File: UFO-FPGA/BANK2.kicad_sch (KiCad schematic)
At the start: 12 parts, among them U1 ICE40HX8K-BG121

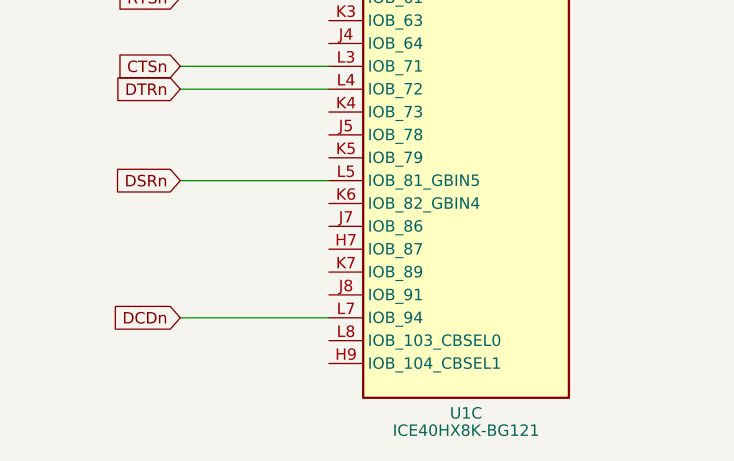
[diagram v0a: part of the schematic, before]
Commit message: PCB planes
Added:
added Power plane +1v2, +3v3 and +5v on layer 4
Ground plane on layer 2 and 5
Added signal layer 1,3 and 6
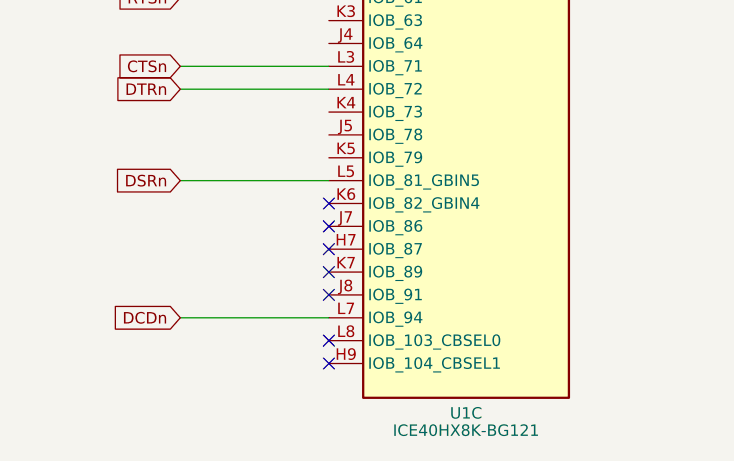
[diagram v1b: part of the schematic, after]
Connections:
- no-connect marks 0 -> 7
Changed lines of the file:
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@@
   (junction (at 161.925 52.07) (diameter 0) (color 0 0 0 0)
   )
+  (no_connect (at 111.125 123.19))
+  (no_connect (at 111.125 125.73))
+  (no_connect (at 111.125 115.57))
+  (no_connect (at 111.125 110.49))
+  (no_connect (at 111.125 113.03))
+  (no_connect (at 111.125 107.95))
+  (no_connect (at 111.125 118.11))
   (wire (pts (xy 94.615 80.01) (xy 111.125 80.01))
     (stroke (width 0) (type default))

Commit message: PCB
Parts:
- TP7, TP8: footprint TestPoint:TestPoint_Keystone_5000-5004_Miniature -> TestPoint:TestPoint_Pad_1.5x1.5mm
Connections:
- net +1V2 is gone; now on net +3V3: R25.1
- net CTSn: no longer U1.L3 (IOB_71)
- net DCDn: no longer U1.L7 (IOB_94)
- net DSRn: no longer U1.L5 (IOB_81_GBIN5)
- net DTRn: no longer U1.L4 (IOB_72)
- net RS232_Rx_TTL: no longer U1.L1 (IOB_56)
- net RTSn: no longer U1.L2 (IOB_61)
- no-connect marks 7 -> 13
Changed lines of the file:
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@@
   )
   (no_connect (at 111.125 123.19))
+  (no_connect (at 111.125 102.87))
   (no_connect (at 111.125 125.73))
+  (no_connect (at 111.125 87.63))
   (no_connect (at 111.125 115.57))
   (no_connect (at 111.125 110.49))
+  (no_connect (at 111.125 107.95))
   (no_connect (at 111.125 113.03))
-  (no_connect (at 111.125 107.95))
+  (no_connect (at 111.125 100.33))
+  (no_connect (at 111.125 90.17))
+  (no_connect (at 111.125 82.55))
   (no_connect (at 111.125 118.11))
+  (no_connect (at 111.125 97.79))
   (wire (pts (xy 94.615 80.01) (xy 111.125 80.01))
     (stroke (width 0) (type default))
@@
     (stroke (width 0) (type default))
   )
+  (wire (pts (xy 174.625 52.07) (xy 173.355 52.07))
+    (stroke (width 0) (type default))
+  )
+  (wire (pts (xy 139.065 52.07) (xy 126.365 52.07))
+    (stroke (width 0) (type default))
+  )
+  (wire (pts (xy 94.615 105.41) (xy 111.125 105.41))
+    (stroke (width 0) (type default))
+  )
+  (wire (pts (xy 161.925 52.07) (xy 150.495 52.07))
+    (stroke (width 0) (type default))
+  )
+  (wire (pts (xy 94.615 120.65) (xy 111.125 120.65))
+    (stroke (width 0) (type default))
+  )
+  (wire (pts (xy 94.615 72.39) (xy 102.235 72.39))
+    (stroke (width 0) (type default))
+  )
+  (wire (pts (xy 161.925 59.69) (xy 173.355 59.69))
+    (stroke (width 0) (type default))
+  )
+  (wire (pts (xy 150.495 52.07) (xy 139.065 52.07))
+    (stroke (width 0) (type default))
+  )
+  (wire (pts (xy 178.435 60.325) (xy 178.435 62.865))
+    (stroke (width 0) (type default))
+  )
+  (wire (pts (xy 102.235 72.39) (xy 111.125 72.39))
+    (stroke (width 0) (type default))
+  )
+  (wire (pts (xy 94.615 92.71) (xy 111.125 92.71))
+    (stroke (width 0) (type default))
+  )
+  (wire (pts (xy 150.495 59.69) (xy 139.065 59.69))
+    (stroke (width 0) (type default))
+  )
   (wire (pts (xy 192.405 41.91) (xy 192.405 52.07))
-    (stroke (width 0) (type default))
-  )
-  (wire (pts (xy 174.625 52.07) (xy 173.355 52.07))
-    (stroke (width 0) (type default))
-  )
-  (wire (pts (xy 139.065 52.07) (xy 126.365 52.07))
-    (stroke (width 0) (type default))
-  )
-  (wire (pts (xy 94.615 105.41) (xy 111.125 105.41))
-    (stroke (width 0) (type default))
-  )
-  (wire (pts (xy 161.925 52.07) (xy 150.495 52.07))
-    (stroke (width 0) (type default))
-  )
-  (wire (pts (xy 94.615 120.65) (xy 111.125 120.65))
-    (stroke (width 0) (type default))
-  )
-  (wire (pts (xy 94.615 72.39) (xy 102.235 72.39))
-    (stroke (width 0) (type default))
-  )
-  (wire (pts (xy 161.925 59.69) (xy 173.355 59.69))
-    (stroke (width 0) (type default))
-  )
-  (wire (pts (xy 150.495 52.07) (xy 139.065 52.07))
-    (stroke (width 0) (type default))
-  )
-  (wire (pts (xy 178.435 60.325) (xy 178.435 62.865))
-    (stroke (width 0) (type default))
-  )
-  (wire (pts (xy 102.235 72.39) (xy 111.125 72.39))
-    (stroke (width 0) (type default))
-  )
-  (wire (pts (xy 94.615 92.71) (xy 111.125 92.71))
-    (stroke (width 0) (type default))
-  )
-  (wire (pts (xy 150.495 59.69) (xy 139.065 59.69))
     (stroke (width 0) (type default))
   )
@@
     (effects (font (size 1.27 1.27)) (justify left bottom))
   )
-  (global_label "CTSn" (shape input) (at 94.615 92.71 180) (fields_autoplaced)
+  (global_label "CTSn" (shape input) (at 86.36 92.71 180) (fields_autoplaced)
     (effects (font (size 1.27 1.27)) (justify right))
-    (property "Intersheetrefs" "${INTERSHEET_REFS}" (at 87.1131 92.71 0)
+    (property "Intersheetrefs" "${INTERSHEET_REFS}" (at 78.8581 92.71 0)
       (effects (font (size 1.27 1.27)) (justify right) hide)
     )
   )
-  (global_label "DCDn" (shape input) (at 94.615 120.65 180) (fields_autoplaced)
+  (global_label "DCDn" (shape input) (at 86.36 120.65 180) (fields_autoplaced)
     (effects (font (size 1.27 1.27)) (justify right))
-    (property "Intersheetrefs" "${INTERSHEET_REFS}" (at 86.7502 120.65 0)
+    (property "Intersheetrefs" "${INTERSHEET_REFS}" (at 78.4952 120.65 0)
       (effects (font (size 1.27 1.27)) (justify right) hide)
     )
@@
     )
   )
-  (global_label "DTRn" (shape input) (at 94.615 95.25 180) (fields_autoplaced)
+  (global_label "DTRn" (shape input) (at 86.36 95.25 180) (fields_autoplaced)
     (effects (font (size 1.27 1.27)) (justify right))
-    (property "Intersheetrefs" "${INTERSHEET_REFS}" (at 87.0526 95.25 0)
+    (property "Intersheetrefs" "${INTERSHEET_REFS}" (at 78.7976 95.25 0)
       (effects (font (size 1.27 1.27)) (justify right) hide)
     )
   )
-  (global_label "RS232_Rx_TTL" (shape input) (at 94.615 80.01 180) (fields_autoplaced)
+  (global_label "RS232_Rx_TTL" (shape input) (at 86.36 80.01 180) (fields_autoplaced)
     (effects (font (size 1.27 1.27)) (justify right))
-    (property "Intersheetrefs" "${INTERSHEET_REFS}" (at 78.4046 80.01 0)
+    (property "Intersheetrefs" "${INTERSHEET_REFS}" (at 70.1496 80.01 0)
       (effects (font (size 1.27 1.27)) (justify right) hide)
     )
   )
-  (global_label "DSRn" (shape input) (at 94.615 105.41 180) (fields_autoplaced)
+  (global_label "DSRn" (shape input) (at 86.36 105.41 180) (fields_autoplaced)
     (effects (font (size 1.27 1.27)) (justify right))
-    (property "Intersheetrefs" "${INTERSHEET_REFS}" (at 86.8107 105.41 0)
+    (property "Intersheetrefs" "${INTERSHEET_REFS}" (at 78.5557 105.41 0)
       (effects (font (size 1.27 1.27)) (justify right) hide)
     )
   )
-  (global_label "RTSn" (shape input) (at 94.615 85.09 180) (fields_autoplaced)
+  (global_label "RTSn" (shape input) (at 86.36 85.09 180) (fields_autoplaced)
     (effects (font (size 1.27 1.27)) (justify right))
-    (property "Intersheetrefs" "${INTERSHEET_REFS}" (at 87.1131 85.09 0)
+    (property "Intersheetrefs" "${INTERSHEET_REFS}" (at 78.8581 85.09 0)
       (effects (font (size 1.27 1.27)) (justify right) hide)
     )
@@
     )
   )
+  (symbol (lib_id "power:+3V3") (at 192.405 41.91 0) (unit 1)
+    (in_bom yes) (on_board yes) (dnp no) (fields_autoplaced)
+    (property "Reference" "#PWR062" (at 192.405 45.72 0)
+      (effects (font (size 1.27 1.27)) hide)
+    )
+    (property "Value" "+3V3" (at 192.405 38.4081 0)
+      (effects (font (size 1.27 1.27)))
+    )
+    (property "Footprint" "" (at 192.405 41.91 0)
+      (effects (font (size 1.27 1.27)) hide)
+    )
+    (property "Datasheet" "" (at 192.405 41.91 0)
+      (effects (font (size 1.27 1.27)) hide)
+    )
+    (pin "1")
+    (instances
+      (project "UFO-FPGA"
+        (path "/b3168f6a-c732-41d3-aeeb-d97dd2f1bb65/03eb349d-f783-448d-a9ad-735fd21dbf61"
+          (reference "#PWR062") (unit 1)
+        )
+        (path "/b3168f6a-c732-41d3-aeeb-d97dd2f1bb65/6f7e0d88-d92b-4c4f-9dc8-64721cd46d41"
+          (reference "#PWR076") (unit 1)
+        )
+      )
+    )
+  )
   (symbol (lib_id "Device:C") (at 139.065 55.88 0) (mirror y) (unit 1)
     (in_bom yes) (on_board yes) (dnp no) (fields_autoplaced)
@@
         (path "/b3168f6a-c732-41d3-aeeb-d97dd2f1bb65/6f7e0d88-d92b-4c4f-9dc8-64721cd46d41"
           (reference "R27") (unit 1)
-        )
-      )
-    )
-  )
-  (symbol (lib_id "power:+1V2") (at 192.405 41.91 0) (unit 1)
-    (in_bom yes) (on_board yes) (dnp no) (fields_autoplaced)
-    (property "Reference" "#PWR024" (at 192.405 45.72 0)
-      (effects (font (size 1.27 1.27)) hide)
-    )
-    (property "Value" "+1V2" (at 192.405 38.4081 0)
-      (effects (font (size 1.27 1.27)))
-    )
-    (property "Footprint" "" (at 192.405 41.91 0)
-      (effects (font (size 1.27 1.27)) hide)
-    )
-    (property "Datasheet" "" (at 192.405 41.91 0)
-      (effects (font (size 1.27 1.27)) hide)
-    )
-    (pin "1")
-    (instances
-      (project "UFO-FPGA"
-        (path "/b3168f6a-c732-41d3-aeeb-d97dd2f1bb65/a9a0295d-b075-4952-a5ba-04debc5f691c"
-          (reference "#PWR024") (unit 1)
-        )
-        (path "/b3168f6a-c732-41d3-aeeb-d97dd2f1bb65/03eb349d-f783-448d-a9ad-735fd21dbf61"
-          (reference "#PWR027") (unit 1)
-        )
-        (path "/b3168f6a-c732-41d3-aeeb-d97dd2f1bb65/6f7e0d88-d92b-4c4f-9dc8-64721cd46d41"
-          (reference "#PWR078") (unit 1)
         )
       )
@@
       (effects (font (size 1.27 1.27)) (justify left))
     )
-    (property "Footprint" "TestPoint:TestPoint_Keystone_5000-5004_Miniature" (at 179.705 52.07 0)
+    (property "Footprint" "TestPoint:TestPoint_Pad_1.5x1.5mm" (at 179.705 52.07 0)
       (effects (font (size 1.27 1.27)) hide)
     )
@@
       (effects (font (size 1.27 1.27)) (justify right))
     )
-    (property "Footprint" "TestPoint:TestPoint_Keystone_5000-5004_Miniature" (at 97.155 72.39 0)
-      (effects (font (size 1.27 1.27)) hide)
-    )
+    (property "Footprint" "TestPoint:TestPoint_Pad_1.5x1.5mm" (at 97.155 72.39 0)
+      (effects (font (size 1.27 1.27)) hide)
+    )

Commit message: PCB
many pcb changes
-started routing
-added vias
-power planes
-ground planes
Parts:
- removed C17 (x3): 100nF, Capacitor_SMD:C_0805_2012Metric_Pad1.18x1.45mm_HandSolder, symbol Device:C
- removed R25: 130R, Resistor_SMD:R_0805_2012Metric_Pad1.20x1.40mm_HandSolder, symbol Device:R
- removed R25: 1R, Resistor_SMD:R_0805_2012Metric_Pad1.20x1.40mm_HandSolder, symbol Device:R
- added C17: 200nF, Capacitor_SMD:C_0805_2012Metric_Pad1.18x1.45mm_HandSolder, symbol Device:C
- added R29: 0, Resistor_SMD:R_0805_2012Metric_Pad1.20x1.40mm_HandSolder, symbol Device:R
- C18: value 100nF -> 200nF
- R25: value 510R -> 690R
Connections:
- net +3V3: now also R29.2
- net GND: now also C17.2
- net ICE_CDONE: now also R25.2
- net VCCIO_2: now also C17.1, R29.1
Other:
- moved on the sheet: R25

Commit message: pcb prog redesign
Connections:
- net ICE_CLK: now reaches U1.K6 (IOB_82_GBIN4)
- no-connect marks 13 -> 12
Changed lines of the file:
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@@
   (no_connect (at 111.125 115.57))
   (no_connect (at 111.125 110.49))
-  (no_connect (at 111.125 107.95))
   (no_connect (at 111.125 113.03))
   (no_connect (at 111.125 100.33))
@@
   )
   (wire (pts (xy 189.23 52.07) (xy 192.405 52.07))
+    (stroke (width 0) (type default))
+  )
+  (wire (pts (xy 86.36 107.95) (xy 111.125 107.95))
     (stroke (width 0) (type default))
   )
@@
       (effects (font (size 1.27 1.27)) (justify right) hide)
     )
+  )
+  (global_label "ICE_CLK" (shape input) (at 86.36 107.95 180) (fields_autoplaced)
+    (effects (font (size 1.27 1.27)) (justify right))
+    (property "Intersheetrefs" "${INTERSHEET_REFS}" (at 75.8947 107.95 0)
+      (effects (font (size 1.27 1.27)) (justify right) hide)
+    )

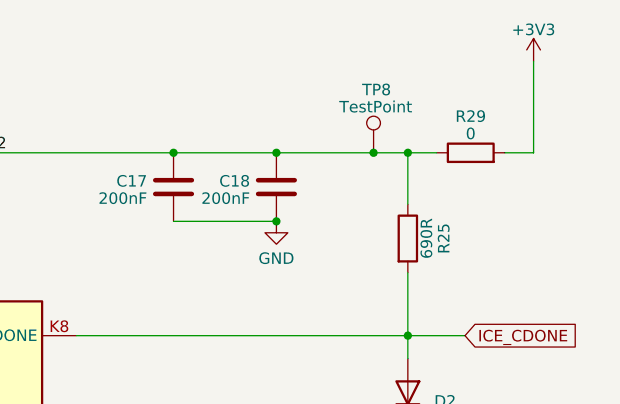
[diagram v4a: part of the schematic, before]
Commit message: pcb placement
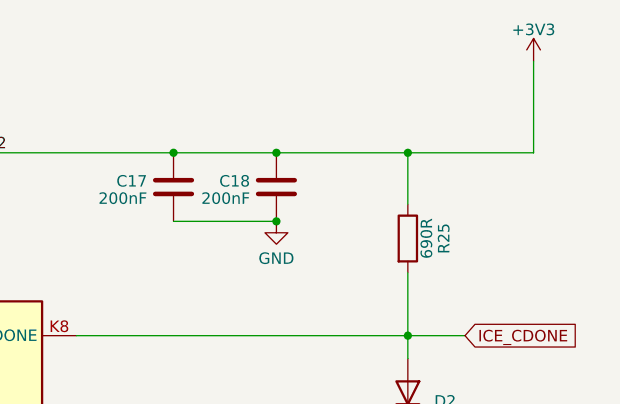
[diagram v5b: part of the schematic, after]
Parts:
- removed R29: 0, Resistor_SMD:R_0805_2012Metric_Pad1.20x1.40mm_HandSolder, symbol Device:R
- removed TP8: TestPoint, TestPoint:TestPoint_Pad_1.5x1.5mm, symbol Connector:TestPoint
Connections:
- net VCCIO_2 is gone; now on net +3V3: C17.1, C18.1, R25.1, U1.H6 (VCCIO_2)
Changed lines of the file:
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@@
   (junction (at 178.435 52.07) (diameter 0) (color 0 0 0 0)
-  )
-  (junction (at 174.625 52.07) (diameter 0) (color 0 0 0 0)
   )
   (junction (at 152.4 52.07) (diameter 0) (color 0 0 0 0)
@@
     (stroke (width 0) (type default))
   )
-  (wire (pts (xy 189.23 52.07) (xy 192.405 52.07))
-    (stroke (width 0) (type default))
-  )
   (wire (pts (xy 86.36 107.95) (xy 111.125 107.95))
     (stroke (width 0) (type default))
@@
     (stroke (width 0) (type default))
   )
-  (wire (pts (xy 163.83 52.07) (xy 174.625 52.07))
-    (stroke (width 0) (type default))
-  )
-  (wire (pts (xy 174.625 52.07) (xy 178.435 52.07))
+  (wire (pts (xy 163.83 52.07) (xy 178.435 52.07))
     (stroke (width 0) (type default))
   )
@@
     (stroke (width 0) (type default))
   )
-  (wire (pts (xy 178.435 52.07) (xy 181.61 52.07))
+  (wire (pts (xy 178.435 52.07) (xy 192.405 52.07))
     (stroke (width 0) (type default))
   )
@@
     )
   )
-  (symbol (lib_id "Device:R") (at 185.42 52.07 90) (unit 1)
-    (in_bom yes) (on_board yes) (dnp no) (fields_autoplaced)
-    (property "Reference" "R29" (at 185.42 48.0441 90)
-      (effects (font (size 1.27 1.27)))
-    )
-    (property "Value" "0" (at 185.42 49.9651 90)
-      (effects (font (size 1.27 1.27)))
-    )
-    (property "Footprint" "Resistor_SMD:R_0805_2012Metric_Pad1.20x1.40mm_HandSolder" (at 185.42 53.848 90)
-      (effects (font (size 1.27 1.27)) hide)
-    )
-    (property "Datasheet" "~" (at 185.42 52.07 0)
-      (effects (font (size 1.27 1.27)) hide)
-    )
-    (pin "1")
-    (pin "2")
-    (instances
-      (project "UFO-FPGA"
-        (path "/b3168f6a-c732-41d3-aeeb-d97dd2f1bb65/f54d4357-d916-4d6b-afb9-9dd5f65d1cf7"
-          (reference "R29") (unit 1)
-        )
-        (path "/b3168f6a-c732-41d3-aeeb-d97dd2f1bb65/6f7e0d88-d92b-4c4f-9dc8-64721cd46d41"
-          (reference "R30") (unit 1)
-        )
-      )
-    )
-  )
   (symbol (lib_id "Device:R") (at 102.235 67.31 0) (unit 1)
     (in_bom yes) (on_board yes) (dnp no) (fields_autoplaced)
@@
         )
       )
-    )
-  )
-  (symbol (lib_id "Connector:TestPoint") (at 174.625 52.07 0) (unit 1)
-    (in_bom yes) (on_board yes) (dnp no)
-    (property "Reference" "TP8" (at 173.355 45.085 0)
-      (effects (font (size 1.27 1.27)) (justify left))
-    )
-    (property "Value" "TestPoint" (at 170.815 46.99 0)
-      (effects (font (size 1.27 1.27)) (justify left))
-    )
-    (property "Footprint" "TestPoint:TestPoint_Pad_1.5x1.5mm" (at 179.705 52.07 0)
-      (effects (font (size 1.27 1.27)) hide)
-    )
-    (property "Datasheet" "~" (at 179.705 52.07 0)
-      (effects (font (size 1.27 1.27)) hide)
-    )
-    (pin "1")
-    (instances
-      (project "UFO-FPGA"
-        (path "/b3168f6a-c732-41d3-aeeb-d97dd2f1bb65/6f7e0d88-d92b-4c4f-9dc8-64721cd46d41"
-          (reference "TP8") (unit 1)
-        )
-        (path "/b3168f6a-c732-41d3-aeeb-d97dd2f1bb65/a9a0295d-b075-4952-a5ba-04debc5f691c"
-          (reference "TP5") (unit 1)
-        )
-      )

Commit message: pcb 0603
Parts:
- C17, C18: footprint Capacitor_SMD:C_0805_2012Metric_Pad1.18x1.45mm_HandSolder -> Capacitor_SMD:C_0603_1608Metric_Pad1.08x0.95mm_HandSolder
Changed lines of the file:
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@@
       (effects (font (size 1.27 1.27)) (justify left))
     )
-    (property "Footprint" "Capacitor_SMD:C_0805_2012Metric_Pad1.18x1.45mm_HandSolder" (at 162.8648 59.69 0)
+    (property "Footprint" "Capacitor_SMD:C_0603_1608Metric_Pad1.08x0.95mm_HandSolder" (at 162.8648 59.69 0)
       (effects (font (size 1.27 1.27)) hide)
     )
@@
       (effects (font (size 1.27 1.27)) (justify left))
     )
-    (property "Footprint" "Capacitor_SMD:C_0805_2012Metric_Pad1.18x1.45mm_HandSolder" (at 151.4348 59.69 0)
-      (effects (font (size 1.27 1.27)) hide)
-    )
+    (property "Footprint" "Capacitor_SMD:C_0603_1608Metric_Pad1.08x0.95mm_HandSolder" (at 151.4348 59.69 0)
+      (effects (font (size 1.27 1.27)) hide)
+    )

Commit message: 0603
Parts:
- R27: footprint Resistor_SMD:R_0805_2012Metric_Pad1.20x1.40mm_HandSolder -> Resistor_SMD:R_0603_1608Metric_Pad0.98x0.95mm_HandSolder
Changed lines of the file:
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@@
       (effects (font (size 1.27 1.27)) (justify left))
     )
-    (property "Footprint" "Resistor_SMD:R_0805_2012Metric_Pad1.20x1.40mm_HandSolder" (at 100.457 67.31 90)
+    (property "Footprint" "Resistor_SMD:R_0603_1608Metric_Pad0.98x0.95mm_HandSolder" (at 100.457 67.31 90)
       (effects (font (size 1.27 1.27)) hide)
     )

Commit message: pcb
added John zendong
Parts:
- removed D2: GREEN, LED_SMD:LED_0805_2012Metric_Pad1.15x1.40mm_HandSolder, symbol Device:LED
- removed R25: 690R, Resistor_SMD:R_0805_2012Metric_Pad1.20x1.40mm_HandSolder, symbol Device:R
- removed R27: 10K, Resistor_SMD:R_0603_1608Metric_Pad0.98x0.95mm_HandSolder, symbol Device:R
- removed TP7: TestPoint, TestPoint:TestPoint_Pad_1.5x1.5mm, symbol Connector:TestPoint
- removed U1: ICE40HX8K-BG121, Package_BGA:BGA-121_9.0x9.0mm_Layout11x11_P0.8mm_Ball0.4mm_Pad0.35mm_NSMD, symbol FPGA_Lattice:ICE40HX8K-BG121
- added U4: ICE40HX4K-TQ144, Package_QFP:TQFP-144_20x20mm_P0.5mm, symbol FPGA_Lattice:ICE40HX4K-TQ144
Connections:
- net +3V3: now also U4.46 (VCCIO_2), U4.57 (VCCIO_2)
- no-connect marks 12 -> 1
